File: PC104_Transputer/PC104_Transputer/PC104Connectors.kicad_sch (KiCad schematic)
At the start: 19 parts, among them J1 Conn_02x32_Odd_Even, J10 Conn_02x30_Row_Letter_First, J2 Conn_02x20_Odd_Even, J4 IRQDMA_JP, J9 Conn_02x30_Row_Letter_First, U5 74LVC1G06

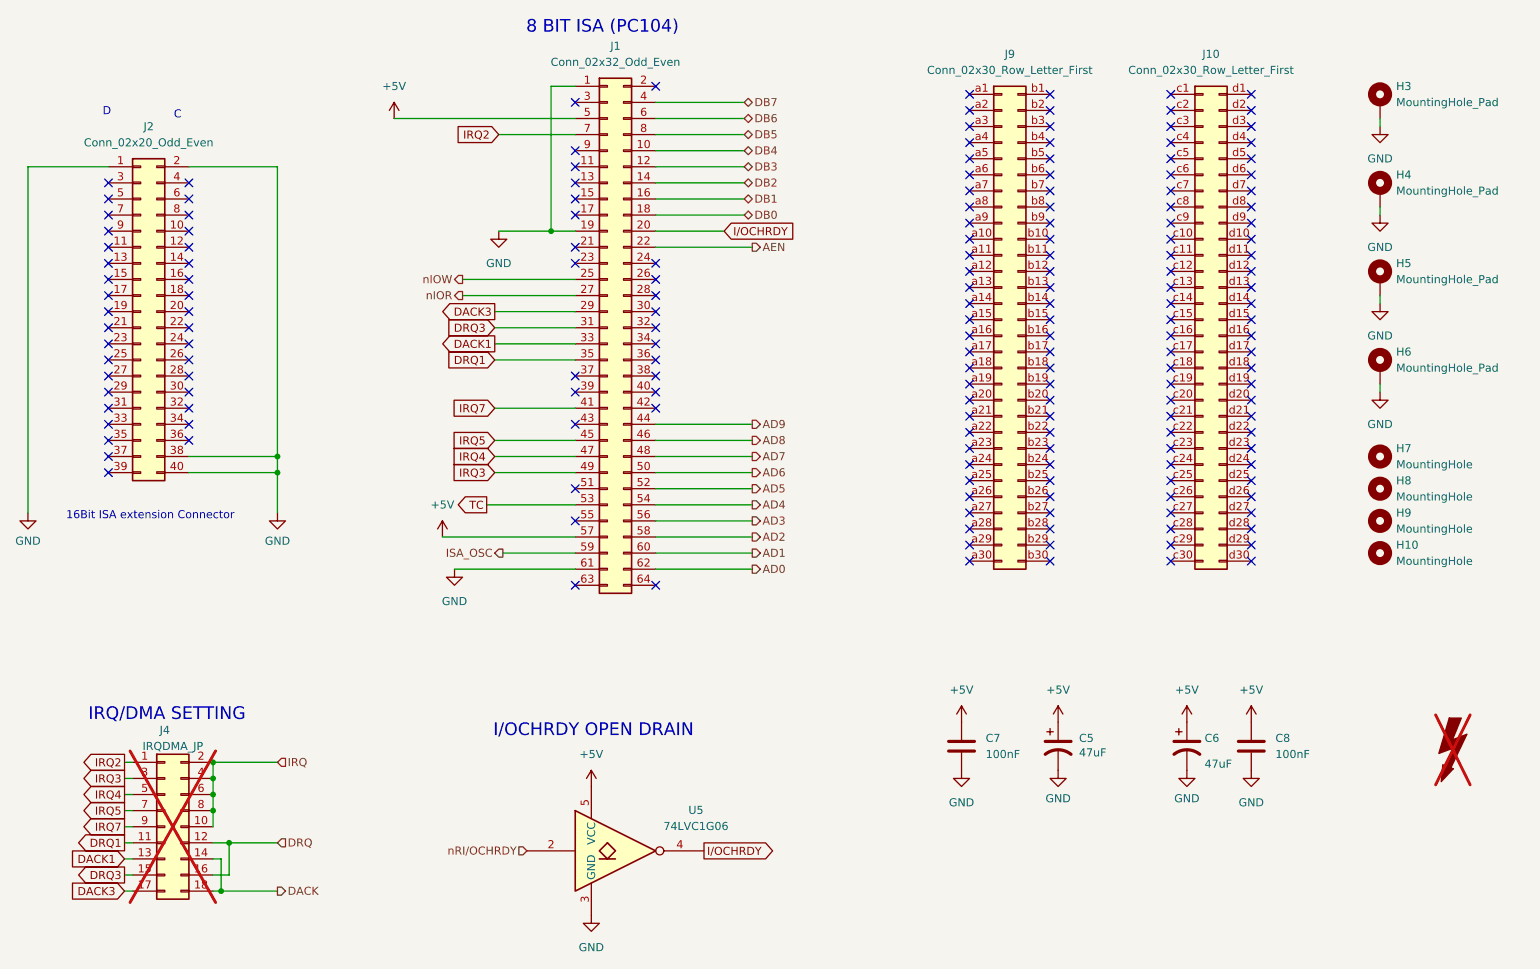
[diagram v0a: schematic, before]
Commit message: Added extra jumpers to transputer board
I also moved the downstream link to the same place as the upstream on the dual TRAM card.
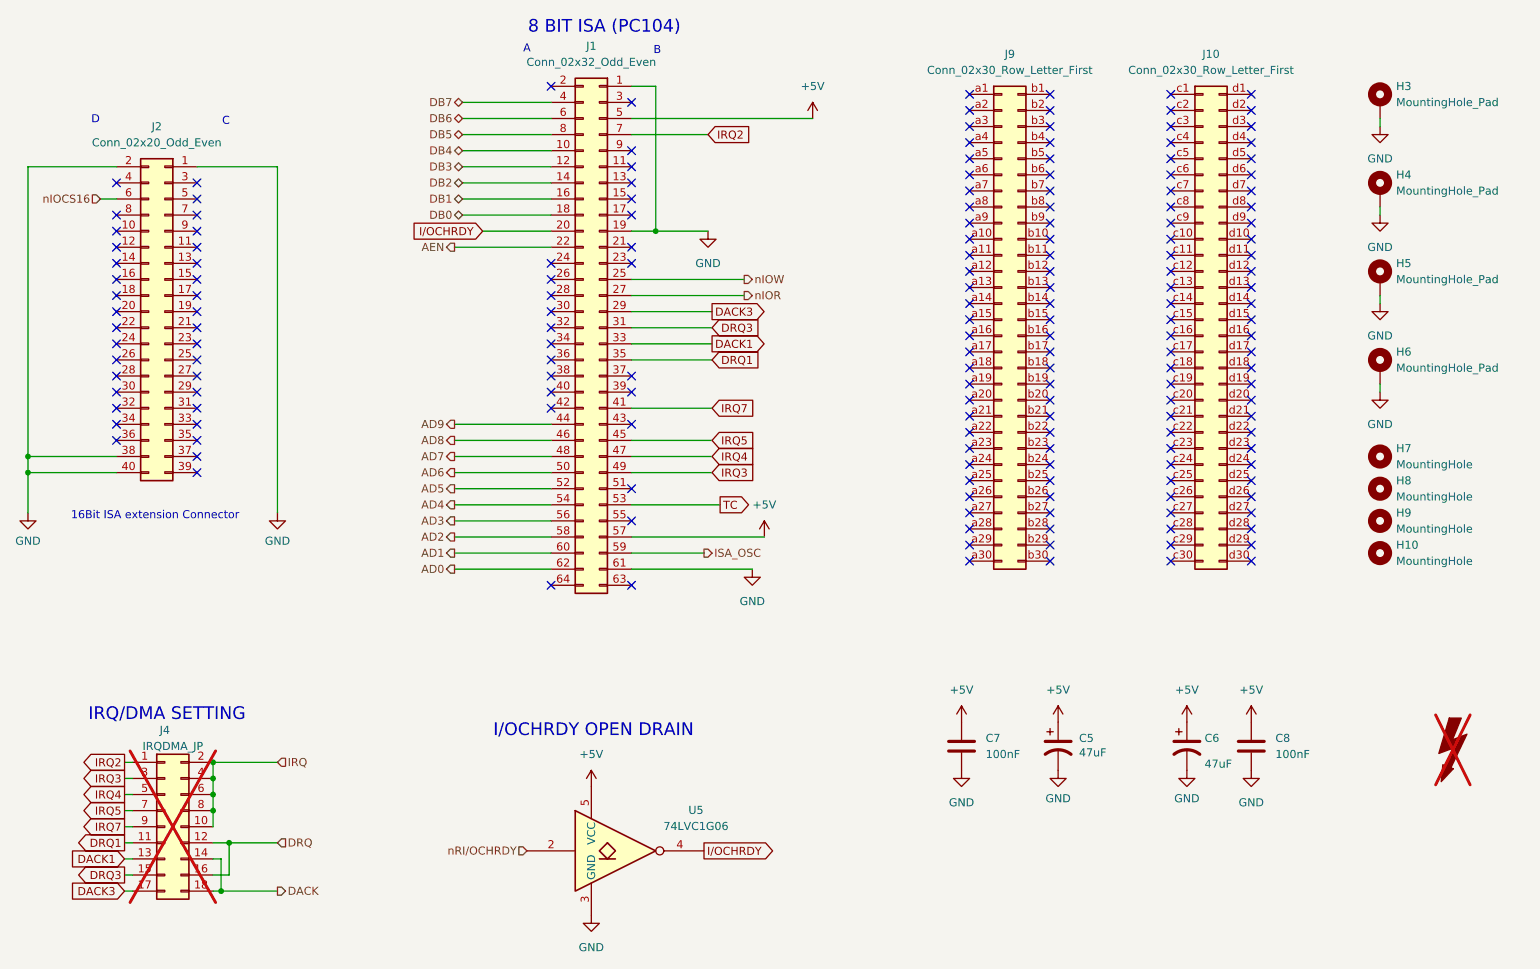
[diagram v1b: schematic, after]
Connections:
- net nIOCS16: now reaches J2.6 (Pin_6)
- no-connect marks 182 -> 181
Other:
- note added: "A"
- note added: "B"
- moved on the sheet: J1, J2
